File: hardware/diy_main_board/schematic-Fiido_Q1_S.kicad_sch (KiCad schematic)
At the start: 12 parts, among them J1 Connector_4, J2 Connector_2, U1 Step-down converter to 3.3V, U2 ESP32C3_SUPER_MINI, U3 SN65HVD230_module

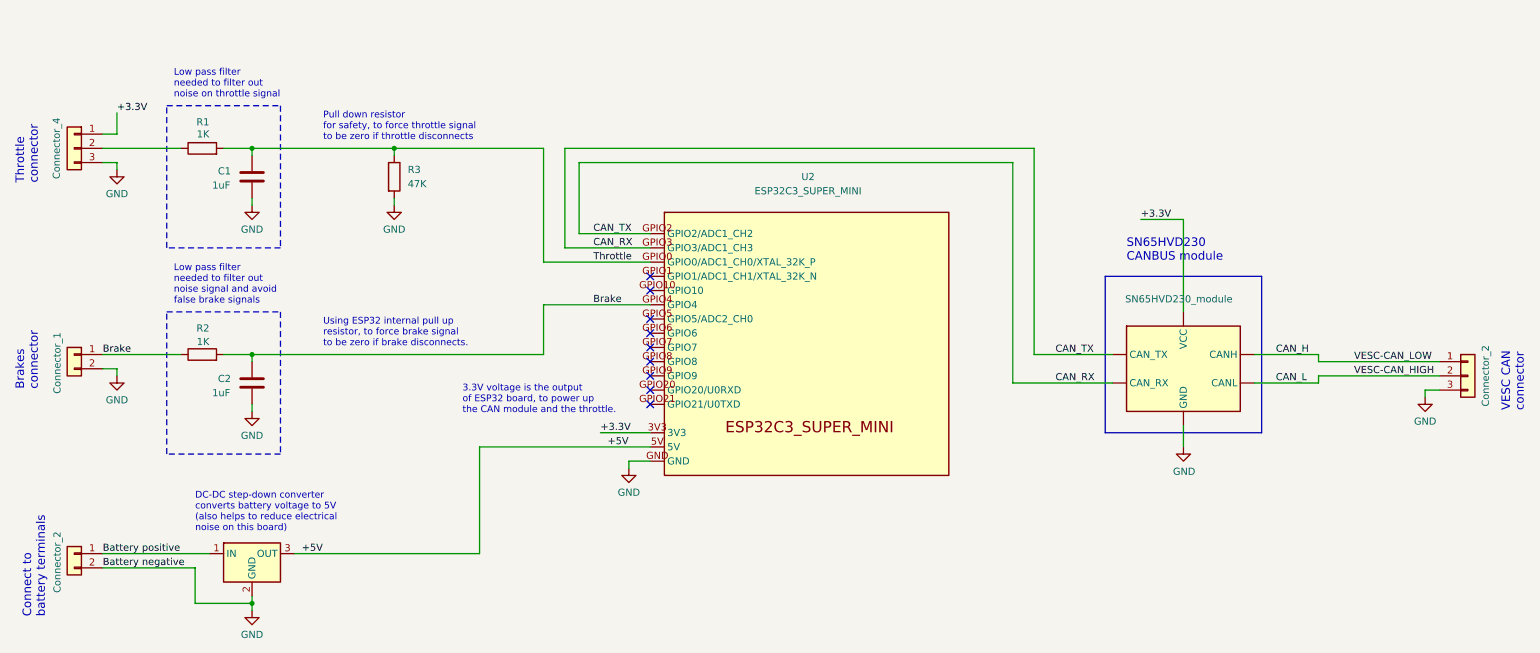
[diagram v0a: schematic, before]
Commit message: Updated motor board, replaced ESP32-C3 for ESP32-S3, due to not enough memory on C3
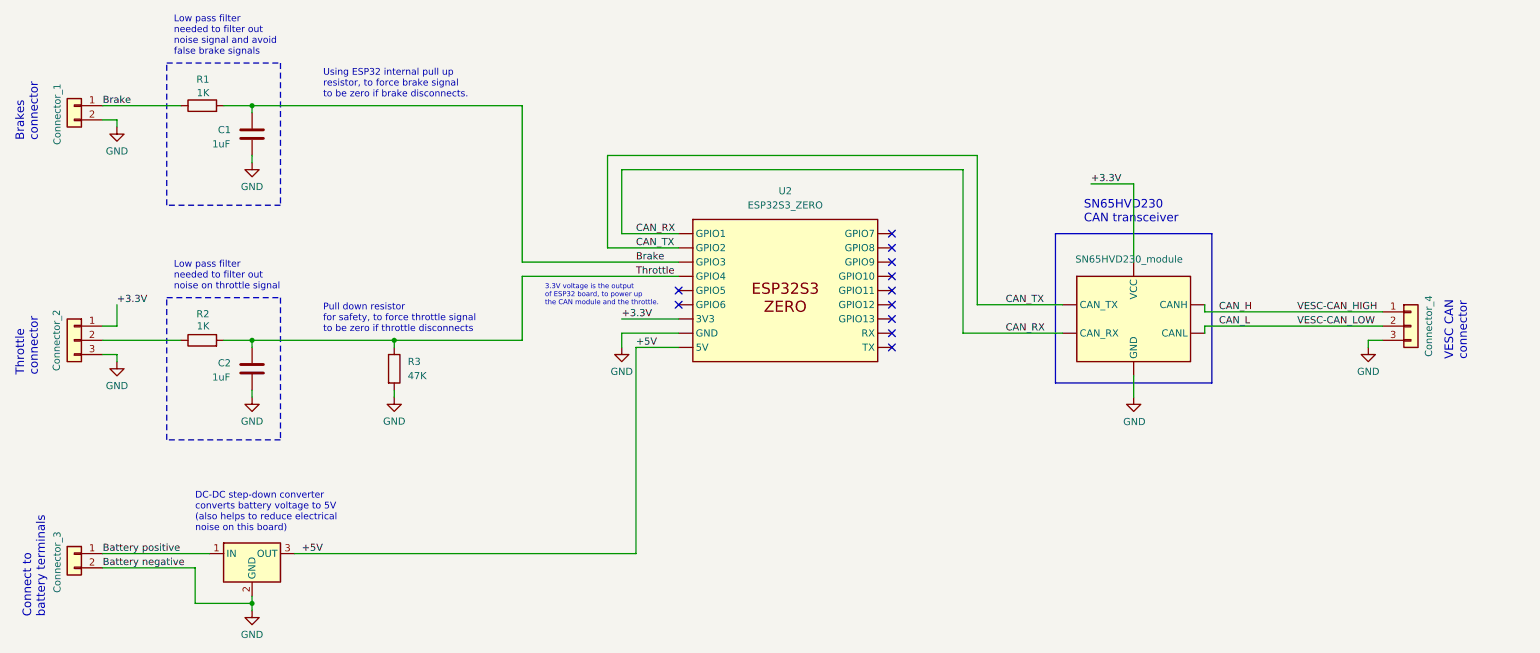
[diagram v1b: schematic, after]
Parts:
- removed U2: ESP32C3_SUPER_MINI, symbol Espressif:ESP32-C3-MINI-1
- added U2: ESP32S3_ZERO, symbol esp32-s3-zero:ESP32-C3-MINI-1
- J1: value Connector_4 -> Connector_2
- J2: value Connector_2 -> Connector_4
- renumbered C2 to C1, C1 to C2, Connector_2 to Connector_3, R2 to R1, R1 to R2
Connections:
- net +3.3V: now also U2. (TX)
- net +5V: now also U2. (TX)
- net Brake: now also U2. (TX)
- net CAN_RX: now also U2. (TX)
- net GND: now also U2. (TX)
- net Throttle: now also U2. (TX)
- new net CAN_TX: U2. (TX), U3. (CANL)
- no-connect marks 9 -> 11
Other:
- note added: "SN65HVD230 CAN transceiver"
- note removed: "SN65HVD230 CANBUS module"
- moved on the sheet: C1, C2, Connector_1, R1, R2, R3

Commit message: Corrected some info about MicroPython with CAN TWAI patch. The firmware now fully works, including read the JBD BMS Blutooth. Organization of folder, new structure. Updated the main board schematic, to correct pins numbers
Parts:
- U3: value SN65HVD230_module -> SN65HVD230
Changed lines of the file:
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@@
 	(text "VESC CAN\nconnector"
 		(exclude_from_sim no)
-		(at 342.9 149.606 90)
+		(at 341.63 144.526 90)
 		(effects
 			(font
@@
 	(text "SN65HVD230\nCAN transceiver"
 		(exclude_from_sim no)
-		(at 274.32 125.222 0)
+		(at 273.05 121.412 0)
 		(effects
 			(font
@@
 	(wire
 		(pts
-			(xy 189.23 113.03) (xy 255.27 113.03)
-		)
-		(stroke
-			(width 0)
-			(type default)
-		)
-	)
-	(wire
-		(pts
-			(xy 283.21 152.4) (xy 283.21 156.21)
+			(xy 189.23 113.03) (xy 254 113.03)
+		)
+		(stroke
+			(width 0)
+			(type default)
+		)
+	)
+	(wire
+		(pts
+			(xy 281.94 147.32) (xy 281.94 151.13)
 		)
 		(stroke
@@
 	(polyline
 		(pts
-			(xy 269.24 127) (xy 297.18 127)
+			(xy 267.97 123.19) (xy 295.91 123.19)
 		)
 		(stroke
@@
 	(polyline
 		(pts
-			(xy 297.18 153.67) (xy 269.24 153.67)
+			(xy 295.91 148.59) (xy 267.97 148.59)
 		)
 		(stroke
@@
 	(wire
 		(pts
-			(xy 255.27 139.7) (xy 270.51 139.7)
+			(xy 254 135.89) (xy 269.24 135.89)
 		)
 		(stroke
@@
 	(polyline
 		(pts
-			(xy 269.24 127) (xy 269.24 153.67)
+			(xy 267.97 123.19) (xy 267.97 148.59)
 		)
 		(stroke
@@
 	(wire
 		(pts
-			(xy 191.77 115.57) (xy 252.73 115.57)
+			(xy 191.77 115.57) (xy 251.46 115.57)
 		)
 		(stroke
@@
 	(wire
 		(pts
-			(xy 255.27 113.03) (xy 255.27 139.7)
+			(xy 254 113.03) (xy 254 135.89)
 		)
 		(stroke
@@
 	(wire
 		(pts
-			(xy 295.91 140.97) (xy 295.91 139.7)
-		)
-		(stroke
-			(width 0)
-			(type default)
-		)
-	)
-	(wire
-		(pts
-			(xy 295.91 143.51) (xy 327.66 143.51)
+			(xy 294.64 138.43) (xy 326.39 138.43)
 		)
 		(stroke
@@
 	(wire
 		(pts
-			(xy 275.59 118.11) (xy 283.21 118.11)
+			(xy 274.32 114.3) (xy 281.94 114.3)
 		)
 		(stroke
@@
 	(wire
 		(pts
-			(xy 252.73 115.57) (xy 252.73 144.78)
-		)
-		(stroke
-			(width 0)
-			(type default)
-		)
-	)
-	(wire
-		(pts
-			(xy 283.21 118.11) (xy 283.21 132.08)
+			(xy 251.46 115.57) (xy 251.46 138.43)
+		)
+		(stroke
+			(width 0)
+			(type default)
+		)
+	)
+	(wire
+		(pts
+			(xy 281.94 114.3) (xy 281.94 127)
 		)
 		(stroke
@@
 	(wire
 		(pts
-			(xy 252.73 144.78) (xy 270.51 144.78)
+			(xy 251.46 138.43) (xy 269.24 138.43)
 		)
 		(stroke
@@
 	(wire
 		(pts
-			(xy 295.91 144.78) (xy 295.91 143.51)
-		)
-		(stroke
-			(width 0)
-			(type default)
-		)
-	)
-	(wire
-		(pts
 			(xy 151.13 146.05) (xy 151.13 147.32)
 		)
@@
 	(wire
 		(pts
-			(xy 325.12 146.05) (xy 325.12 147.32)
+			(xy 323.85 140.97) (xy 323.85 142.24)
 		)
 		(stroke
@@
 	(wire
 		(pts
-			(xy 327.66 146.05) (xy 325.12 146.05)
+			(xy 326.39 140.97) (xy 323.85 140.97)
 		)
 		(stroke
@@
 	(polyline
 		(pts
-			(xy 297.18 127) (xy 297.18 153.67)
+			(xy 295.91 123.19) (xy 295.91 148.59)
 		)
 		(stroke
@@
 	(wire
 		(pts
-			(xy 295.91 140.97) (xy 327.66 140.97)
+			(xy 294.64 135.89) (xy 326.39 135.89)
 		)
 		(stroke
@@
 	)
 	(label "VESC-CAN_LOW"
-		(at 312.42 143.51 0)
+		(at 311.15 138.43 0)
 		(effects
 			(font
@@
 	)
 	(label "CAN_RX"
-		(at 260.35 144.78 0)
+		(at 259.08 138.43 0)
 		(effects
 			(font
@@
 	)
 	(label "+3.3V"
-		(at 275.59 118.11 0)
+		(at 274.32 114.3 0)
 		(effects
 			(font
@@
 	)
 	(label "CAN_L"
-		(at 298.45 143.51 0)
+		(at 297.18 138.43 0)
 		(effects
 			(font
@@
 	)
 	(label "VESC-CAN_HIGH"
-		(at 312.42 140.97 0)
+		(at 311.15 135.89 0)
 		(effects
 			(font
@@
 	)
 	(label "CAN_H"
-		(at 298.45 140.97 0)
+		(at 297.18 135.89 0)
 		(effects
 			(font
@@
 	)
 	(label "CAN_TX"
-		(at 260.35 139.7 0)
+		(at 259.08 135.89 0)
 		(effects
 			(font
@@
 					(size 1.27 1.27)
 				)
+				(hide yes)
 			)
 		)
@@
 	(symbol
 		(lib_id "power:GND")
-		(at 283.21 156.21 0)
+		(at 281.94 151.13 0)
 		(unit 1)
 		(exclude_from_sim no)
@@
 		(dnp no)
 		(property "Reference" "#PWR08"
-			(at 283.21 162.56 0)
+			(at 281.94 157.48 0)
 			(effects
 				(font
@@
 		)
 		(property "Value" "GND"
-			(at 283.337 160.6042 0)
+			(at 282.067 155.5242 0)
 			(effects
 				(font
@@
 		)
 		(property "Footprint" ""
-			(at 283.21 156.21 0)
+			(at 281.94 151.13 0)
 			(effects
 				(font
@@
 		)
 		(property "Datasheet" ""
-			(at 283.21 156.21 0)
+			(at 281.94 151.13 0)
 			(effects
 				(font
@@
 		)
 		(property "Description" ""
-			(at 283.21 156.21 0)
+			(at 281.94 151.13 0)
 			(effects
 				(font
@@
 	(symbol
 		(lib_id "Connector_Generic:Conn_01x03")
-		(at 332.74 143.51 0)
+		(at 331.47 138.43 0)
 		(unit 1)
 		(exclude_from_sim no)
@@
 		(dnp no)
 		(property "Reference" "J2"
-			(at 332.74 136.144 0)
+			(at 331.47 131.064 0)
 			(effects
 				(font
@@
 		)
 		(property "Value" "Connector_4"
-			(at 335.915 143.51 90)
+			(at 334.645 138.43 90)
 			(effects
 				(font
@@
 		)
 		(property "Footprint" ""
-			(at 332.74 143.51 0)
+			(at 331.47 138.43 0)
 			(effects
 				(font
@@
 		)
 		(property "Datasheet" "~"
-			(at 332.74 143.51 0)
+			(at 331.47 138.43 0)
 			(effects
 				(font
@@
 		)
 		(property "Description" ""
-			(at 332.74 143.51 0)
+			(at 331.47 138.43 0)
 			(effects
 				(font
@@
 	(symbol
 		(lib_id "TJA1050:TJA1050_module")
-		(at 283.21 142.24 0)
+		(at 281.94 137.16 0)
 		(unit 1)
 		(exclude_from_sim no)
@@
 		(dnp no)
 		(property "Reference" "U3"
-			(at 285.2294 129.54 0)
+			(at 283.9594 124.46 0)
 			(effects
 				(font
@@
 			)
 		)
-		(property "Value" "SN65HVD230_module"
-			(at 272.796 131.572 0)
+		(property "Value" "SN65HVD230"
+			(at 275.844 127.254 0)
 			(effects
 				(font
@@
 		)
 		(property "Footprint" ""
-			(at 283.21 154.94 0)
+			(at 281.94 149.86 0)
 			(effects
 				(font
@@
 		)
 		(property "Datasheet" ""
-			(at 283.21 142.24 0)
+			(at 281.94 137.16 0)
 			(effects
 				(font
@@
 		)
 		(property "Description" ""
-			(at 283.21 142.24 0)
+			(at 281.94 137.16 0)
 			(effects
 				(font
@@
 	(symbol
 		(lib_id "power:GND")
-		(at 325.12 147.32 0)
+		(at 323.85 142.24 0)
 		(mirror y)
 		(unit 1)
@@
 		(dnp no)
 		(property "Reference" "#PWR09"
-			(at 325.12 153.67 0)
+			(at 323.85 148.59 0)
 			(effects
 				(font
@@
 		)
 		(property "Value" "GND"
-			(at 325.12 151.638 0)
+			(at 323.85 146.558 0)
 			(effects
 				(font
@@
 		)
 		(property "Footprint" ""
-			(at 325.12 147.32 0)
+			(at 323.85 142.24 0)
 			(effects
 				(font
@@
 		)
 		(property "Datasheet" ""
-			(at 325.12 147.32 0)
+			(at 323.85 142.24 0)
 			(effects
 				(font
@@
 		)
 		(property "Description" ""
-			(at 325.12 147.32 0)
-			(effects
-				(font
+			(at 323.85 142.24 0)
+			(effects
+				(font
